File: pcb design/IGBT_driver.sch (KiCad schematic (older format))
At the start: 37 parts, among them Q13 NPN, Q14 PNP, U1 ISO5852S

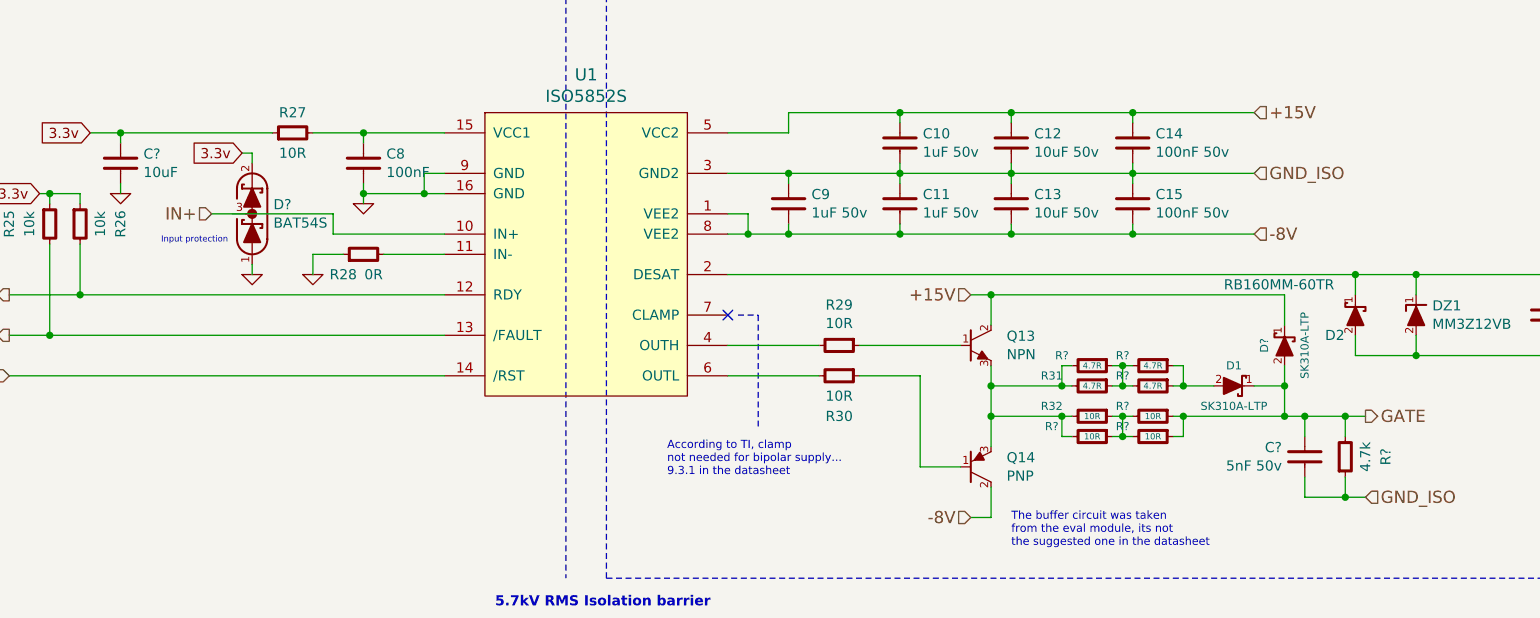
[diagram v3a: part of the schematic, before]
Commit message: Added 3D models, connector, more layout, updated readme
Signed-off-by: Marcos Chaparro <mchaparro@paltatech.com>
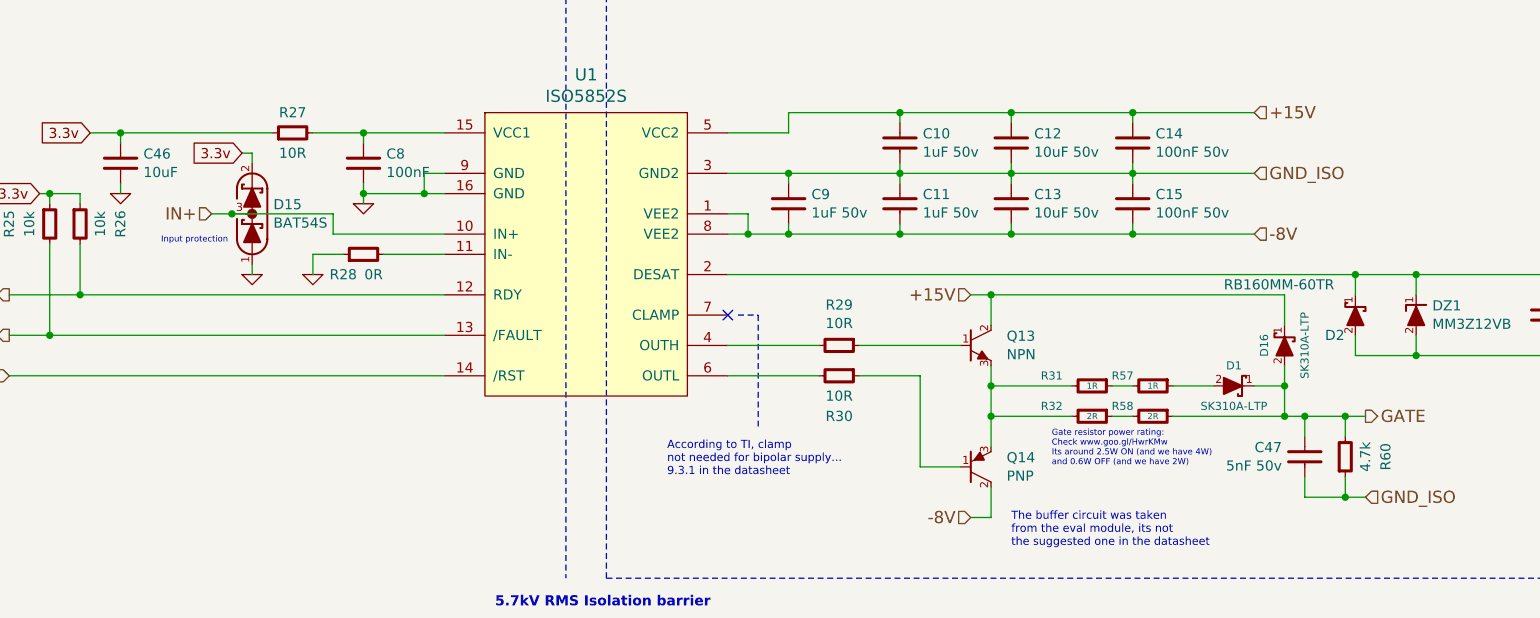
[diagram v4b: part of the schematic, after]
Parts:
- removed R? (x2): 4.7R, IPC7351-Nominal:RESC3225X60, symbol R-0805
- removed R? (x2): 10R, IPC7351-Nominal:RESC3225X60, symbol R-0805
- R31: value 4.7R -> 1R
- R32: value 10R -> 2R
- R57: renamed from R?; value 4.7R -> 1R
- R58: renamed from R?; value 10R -> 2R
- gave numbers to parts that had none: 5
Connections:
- net IN+: now also D15.3 (COM)
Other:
- note added: "Gate resistor power rating:\nCheck www.goo.gl/HwrKMw\nIts around 2.5W ON (and we have 4W)\nand 0.6W OFF (and we have 2W)"
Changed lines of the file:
@@
 	3050 4300 2750 4300
 $Comp
-L GND #PWR01
+L GND #PWR02
 U 1 1 582416B6
 P 2400 4400
-AR Path="/5822D62D/582416B6" Ref="#PWR01"  Part="1"
-AR Path="/5824556D/582416B6" Ref="#PWR014"  Part="1"
-F 0 "#PWR01" H 2400 4400 30  0001 C CNN
+AR Path="/5822D62D/582416B6" Ref="#PWR02"  Part="1"
+AR Path="/5824556D/582416B6" Ref="#PWR017"  Part="1"
+F 0 "#PWR02" H 2400 4400 30  0001 C CNN
 F 1 "GND" H 2400 4330 30  0001 C CNN
 F 2 "" H 2400 4400 60  0000 C CNN
@@
 	2950 3900 2950 4000
 $Comp
-L GND #PWR02
+L GND #PWR03
 U 1 1 58241AEC
 P 2650 4050
-AR Path="/5822D62D/58241AEC" Ref="#PWR02"  Part="1"
-AR Path="/5824556D/58241AEC" Ref="#PWR015"  Part="1"
-F 0 "#PWR02" H 2650 4050 30  0001 C CNN
+AR Path="/5822D62D/58241AEC" Ref="#PWR03"  Part="1"
+AR Path="/5824556D/58241AEC" Ref="#PWR018"  Part="1"
+F 0 "#PWR03" H 2650 4050 30  0001 C CNN
 F 1 "GND" H 2650 3980 30  0001 C CNN
 F 2 "" H 2650 4050 60  0000 C CNN
@@
 AR Path="/5824556D/5824286A" Ref="R48"  Part="1"
 F 0 "R31" V 6200 4750 40  0000 C CNN
-F 1 "4.7R" V 6250 4950 30  0000 C CNN
+F 1 "1R" V 6250 4950 30  0000 C CNN
 F 2 "IPC7351-Nominal:RESC3225X60" H 6250 4950 50  0001 C CNN
 F 3 "" H 6250 5000 60  0000 C CNN
@@
 AR Path="/5824556D/58242871" Ref="R49"  Part="1"
 F 0 "R32" V 6200 4900 40  0000 C CNN
-F 1 "10R" V 6250 5100 30  0000 C CNN
+F 1 "2R" V 6250 5100 30  0000 C CNN
 F 2 "IPC7351-Nominal:RESC3225X60" H 6250 5100 50  0001 C CNN
 F 3 "" H 6250 5150 60  0000 C CNN
@@
 	7300 5500 7300 5400
 $Comp
-L R-0805 R?
+L R-0805 R60
 U 1 1 58308678
 P 7500 5300
-AR Path="/5822D62D/58308678" Ref="R?"  Part="1"
-AR Path="/5824556D/58308678" Ref="R?"  Part="1"
-F 0 "R?" V 7700 5300 50  0000 C CNN
+AR Path="/5822D62D/58308678" Ref="R60"  Part="1"
+AR Path="/5824556D/58308678" Ref="R67"  Part="1"
+F 0 "R60" V 7700 5300 50  0000 C CNN
 F 1 "4.7k" V 7600 5300 50  0000 C CNN
 F 2 "IPC7351-Nominal:RESC2012X50" H 7500 5300 50  0001 C CNN
@@
 $EndBitmap
 $Comp
-L C-0603 C?
+L C-0603 C46
 U 1 1 5830FA22
 P 1450 3850
-AR Path="/5822D62D/5830FA22" Ref="C?"  Part="1"
-AR Path="/5824556D/5830FA22" Ref="C?"  Part="1"
-F 0 "C?" H 1563 3896 50  0000 L CNN
+AR Path="/5822D62D/5830FA22" Ref="C46"  Part="1"
+AR Path="/5824556D/5830FA22" Ref="C48"  Part="1"
+F 0 "C46" H 1563 3896 50  0000 L CNN
 F 1 "10uF" H 1563 3805 50  0000 L CNN
 F 2 "IPC7351-Nominal:CAPC1608X55" H 1450 3850 50  0001 C CNN
@@
 Connection ~ 1450 3700
 $Comp
-L GND #PWR?
+L GND #PWR04
 U 1 1 5830FC3F
 P 1450 4000
-AR Path="/5822D62D/5830FC3F" Ref="#PWR?"  Part="1"
-AR Path="/5824556D/5830FC3F" Ref="#PWR?"  Part="1"
-F 0 "#PWR?" H 1450 4000 30  0001 C CNN
+AR Path="/5822D62D/5830FC3F" Ref="#PWR04"  Part="1"
+AR Path="/5824556D/5830FC3F" Ref="#PWR019"  Part="1"
+F 0 "#PWR04" H 1450 4000 30  0001 C CNN
 F 1 "GND" H 1450 3930 30  0001 C CNN
 F 2 "" H 1450 4000 60  0000 C CNN
@@
 	1450 4000 1450 3950
 $Comp
-L BAT54S D?
+L BAT54S D15
 U 1 1 583100FD
 P 2100 4100
-AR Path="/5822D62D/583100FD" Ref="D?"  Part="1"
-AR Path="/5824556D/583100FD" Ref="D?"  Part="1"
-F 0 "D?" V 2146 3995 50  0000 R CNN
+AR Path="/5822D62D/583100FD" Ref="D15"  Part="1"
+AR Path="/5824556D/583100FD" Ref="D17"  Part="1"
+F 0 "D15" V 2146 3995 50  0000 R CNN
 F 1 "BAT54S" V 2055 3995 50  0000 R CNN
 F 2 "smd-semi:SOT-23" H 2100 3950 60  0001 C CNN
@@
 	2100 3800 2100 3850
 $Comp
-L GND #PWR?
+L GND #PWR05
 U 1 1 58310421
 P 2100 4400
-AR Path="/5822D62D/58310421" Ref="#PWR?"  Part="1"
-AR Path="/5824556D/58310421" Ref="#PWR?"  Part="1"
-F 0 "#PWR?" H 2100 4400 30  0001 C CNN
+AR Path="/5822D62D/58310421" Ref="#PWR05"  Part="1"
+AR Path="/5824556D/58310421" Ref="#PWR020"  Part="1"
+F 0 "#PWR05" H 2100 4400 30  0001 C CNN
 F 1 "GND" H 2100 4330 30  0001 C CNN
 F 2 "" H 2100 4400 60  0000 C CNN
@@
 P 7300 5300
 AR Path="/58232371/58307C69" Ref="C?"  Part="1"
-AR Path="/5822D62D/58307C69" Ref="C?"  Part="1"
-AR Path="/5824556D/58307C69" Ref="C?"  Part="1"
-F 0 "C?" H 7413 5346 50  0000 L CNN
+AR Path="/5822D62D/58307C69" Ref="C47"  Part="1"
+AR Path="/5824556D/58307C69" Ref="C49"  Part="1"
+F 0 "C47" H 7413 5346 50  0000 L CNN
 F 1 "5nF 50v" H 7413 5255 50  0000 L CNN
 F 2 "IPC7351-Nominal:CAPC2012X70" H 7300 5300 50  0001 C CNN
@@
 $EndComp
 $Comp
-L R-0805 R?
-U 1 1 5832B661
-P 6250 4850
-AR Path="/5822D62D/5832B661" Ref="R?"  Part="1"
-AR Path="/5824556D/5832B661" Ref="R?"  Part="1"
-F 0 "R?" V 6200 4700 40  0000 C CNN
-F 1 "4.7R" V 6250 4850 30  0000 C CNN
-F 2 "IPC7351-Nominal:RESC3225X60" H 6250 4850 50  0001 C CNN
-F 3 "" H 6250 4900 60  0000 C CNN
-F 4 "RES SMD 1k 5% [2512]" H 7000 5400 60  0001 C CNN "BOM"
-	1    6250 4850
-	0    1    1    0
-$EndComp
-Wire Wire Line
-	6150 4850 6100 4850
-Wire Wire Line
-	6100 4850 6100 4950
-Connection ~ 6100 4950
-Wire Wire Line
-	6350 4850 6450 4850
-Wire Wire Line
-	6400 4850 6400 4950
-$Comp
-L R-0805 R?
-U 1 1 5832BA90
-P 6250 5200
-AR Path="/5822D62D/5832BA90" Ref="R?"  Part="1"
-AR Path="/5824556D/5832BA90" Ref="R?"  Part="1"
-F 0 "R?" V 6200 5000 40  0000 C CNN
-F 1 "10R" V 6250 5200 30  0000 C CNN
-F 2 "IPC7351-Nominal:RESC3225X60" H 6250 5200 50  0001 C CNN
-F 3 "" H 6250 5250 60  0000 C CNN
-F 4 "RES SMD 1k 5% [2512]" H 7000 5750 60  0001 C CNN "BOM"
-	1    6250 5200
-	0    1    1    0
-$EndComp
-Wire Wire Line
-	6150 5200 6100 5200
-Wire Wire Line
-	6100 5200 6100 5100
-Connection ~ 6100 5100
-Wire Wire Line
-	6350 5200 6450 5200
-Wire Wire Line
-	6400 5200 6400 5100
-$Comp
-L R-0805 R?
-U 1 1 5832CE45
-P 6550 4850
-AR Path="/5822D62D/5832CE45" Ref="R?"  Part="1"
-AR Path="/5824556D/5832CE45" Ref="R?"  Part="1"
-F 0 "R?" V 6500 4700 40  0000 C CNN
-F 1 "4.7R" V 6550 4850 30  0000 C CNN
-F 2 "IPC7351-Nominal:RESC3225X60" H 6550 4850 50  0001 C CNN
-F 3 "" H 6550 4900 60  0000 C CNN
-F 4 "RES SMD 1k 5% [2512]" H 7300 5400 60  0001 C CNN "BOM"
-	1    6550 4850
-	0    1    1    0
-$EndComp
-Connection ~ 6400 4850
-$Comp
-L R-0805 R?
+L R-0805 R57
 U 1 1 5832D091
 P 6550 4950
-AR Path="/5822D62D/5832D091" Ref="R?"  Part="1"
-AR Path="/5824556D/5832D091" Ref="R?"  Part="1"
-F 0 "R?" V 6500 4800 40  0000 C CNN
-F 1 "4.7R" V 6550 4950 30  0000 C CNN
+AR Path="/5822D62D/5832D091" Ref="R57"  Part="1"
+AR Path="/5824556D/5832D091" Ref="R64"  Part="1"
+F 0 "R57" V 6500 4800 40  0000 C CNN
+F 1 "1R" V 6550 4950 30  0000 C CNN
 F 2 "IPC7351-Nominal:RESC3225X60" H 6550 4950 50  0001 C CNN
 F 3 "" H 6550 5000 60  0000 C CNN
@@
 	0    1    1    0
 $EndComp
-Connection ~ 6400 4950
 Wire Wire Line
 	6650 4950 6850 4950
-Wire Wire Line
-	6650 4850 6700 4850
-Wire Wire Line
-	6700 4850 6700 4950
-Connection ~ 6700 4950
 $Comp
-L R-0805 R?
+L R-0805 R58
 U 1 1 5832D475
 P 6550 5100
-AR Path="/5822D62D/5832D475" Ref="R?"  Part="1"
-AR Path="/5824556D/5832D475" Ref="R?"  Part="1"
-F 0 "R?" V 6500 4950 40  0000 C CNN
-F 1 "10R" V 6550 5100 30  0000 C CNN
+AR Path="/5822D62D/5832D475" Ref="R58"  Part="1"
+AR Path="/5824556D/5832D475" Ref="R65"  Part="1"
+F 0 "R58" V 6500 4950 40  0000 C CNN
+F 1 "2R" V 6550 5100 30  0000 C CNN
 F 2 "IPC7351-Nominal:RESC3225X60" H 6550 5100 50  0001 C CNN
 F 3 "" H 6550 5150 60  0000 C CNN
@@
 	0    1    1    0
 $EndComp
-Connection ~ 6400 5100
-$Comp
-L R-0805 R?
-U 1 1 5832D63E
-P 6550 5200
-AR Path="/5822D62D/5832D63E" Ref="R?"  Part="1"
-AR Path="/5824556D/5832D63E" Ref="R?"  Part="1"
-F 0 "R?" V 6500 5050 40  0000 C CNN
-F 1 "10R" V 6550 5200 30  0000 C CNN
-F 2 "IPC7351-Nominal:RESC3225X60" H 6550 5200 50  0001 C CNN
-F 3 "" H 6550 5250 60  0000 C CNN
-F 4 "RES SMD 1k 5% [2512]" H 7300 5750 60  0001 C CNN "BOM"
-	1    6550 5200
-	0    1    1    0
-$EndComp
-Connection ~ 6400 5200
-Wire Wire Line
-	6650 5200 6700 5200
-Wire Wire Line
-	6700 5200 6700 5100
 Connection ~ 7200 5100
-Connection ~ 6700 5100
 Text Notes 4150 5400 0    40   ~ 0
 According to TI, clamp\nnot needed for bipolar supply...\n9.3.1 in the datasheet
@@
 	4600 4600 4600 5150
 $Comp
-L SCHOTTKY D?
+L SCHOTTKY D16
 U 1 1 5833272F
 P 7200 4750
-F 0 "D?" V 7300 4750 40  0000 C CNN
+AR Path="/5822D62D/5833272F" Ref="D16"  Part="1"
+AR Path="/5824556D/5833272F" Ref="D18"  Part="1"
+F 0 "D16" V 7300 4750 40  0000 C CNN
 F 1 "SK310A-LTP" V 7100 4750 40  0000 C CNN
 F 2 "w_smd_diode:do214ac" H 7200 4750 60  0001 C CNN
@@
 	7200 4500 7200 4650
 Connection ~ 5750 4500
+Connection ~ 2000 4100
+Text Notes 6050 5350 0    30   ~ 0
+Gate resistor power rating:\nCheck www.goo.gl/HwrKMw\nIts around 2.5W ON (and we have 4W)\nand 0.6W OFF (and we have 2W)
 $EndSCHEMATC

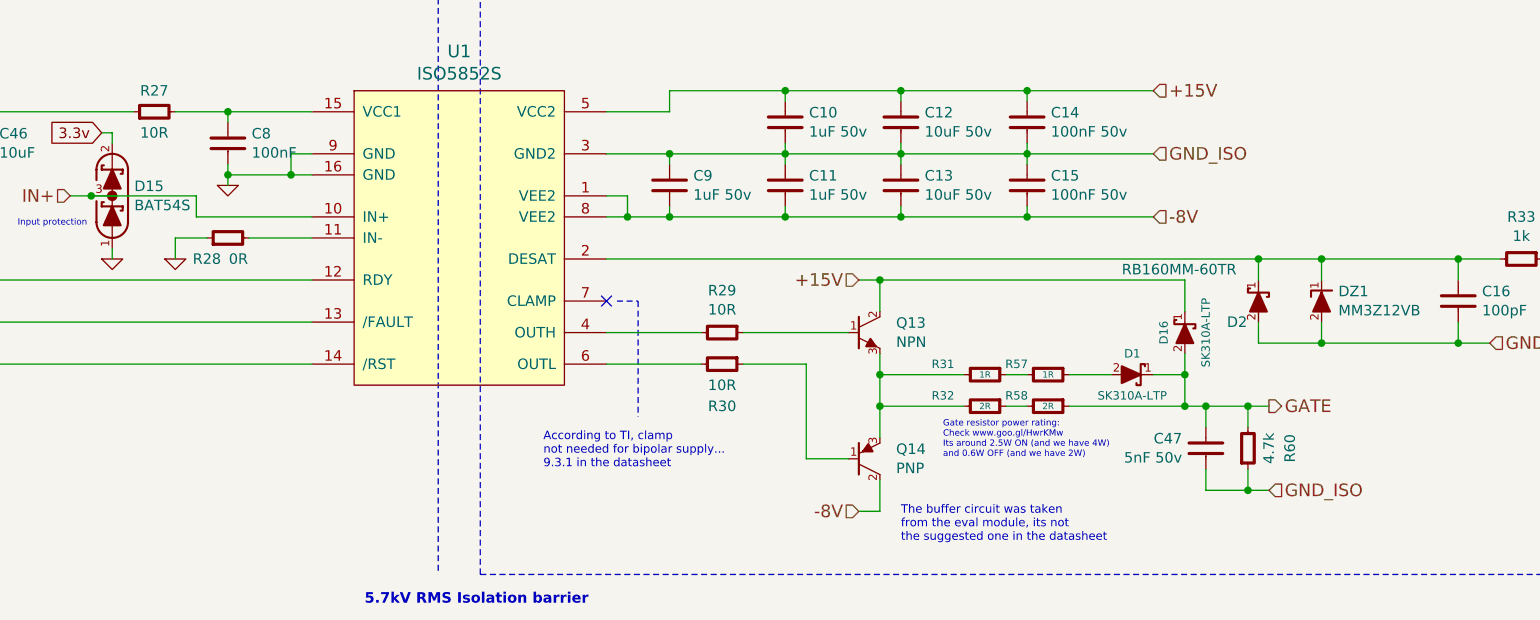
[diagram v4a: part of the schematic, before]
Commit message: Added testpoints
Signed-off-by: Marcos Chaparro <mchaparro@paltatech.com>
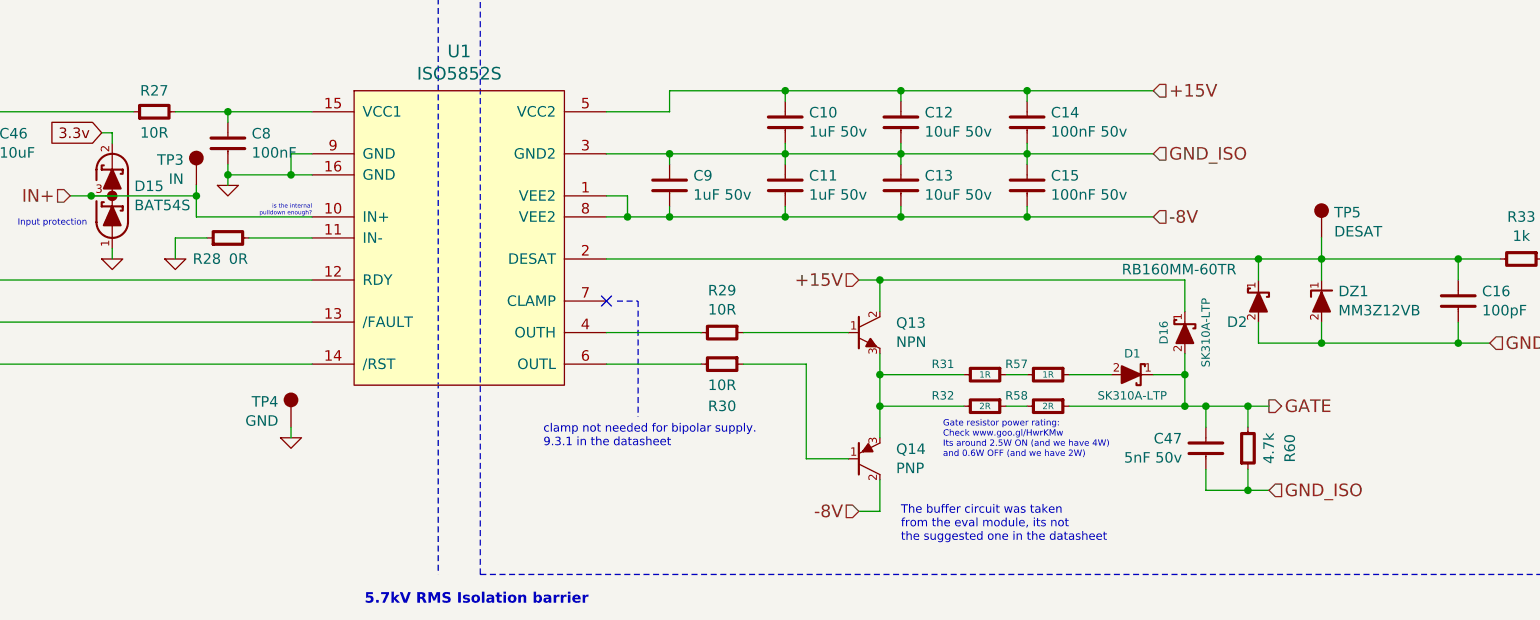
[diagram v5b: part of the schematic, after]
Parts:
- added TP3: IN, conn-test:TEST-SMD-SMALL, symbol TESTPOINT
- added TP4: GND, conn-test:TEST-SMD-SMALL, symbol TESTPOINT
- added TP5: DESAT, conn-test:TEST-SMD-SMALL, symbol TESTPOINT
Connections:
- net GND: now also TP4.1
- net IN+: now also TP3.1
- net at C16.1, D2.1 (K), DZ1.1 (K)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: now also TP5.1
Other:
- note added: "clamp not needed for bipolar supply.\n9.3.1 in the datasheet"
- note added: "is the internal\npulldown enough?"
- note removed: "According to TI, clamp\nnot needed for bipolar supply...\n9.3.1 in the datasheet"

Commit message: Change gate diode direction, I thought Ron should be smaller than Roff, and its not
Signed-off-by: Marcos Chaparro <mchaparro@paltatech.com>
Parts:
- removed R28: 0R, IPC7351-Nominal:RESC1608X50, symbol R-0603
- added J2: DESAT, conn-100mil:CONN-100MIL-F-1x1, symbol CONN-100MIL-F-1x1
- added R?: 10k, IPC7351-Nominal:RESC1608X50, symbol R-0603
- added U?: SN74AUC1G14, smd-semi:SOT-23-5, symbol 741G04-SOT23
- R31, R57: value 1R -> 2R
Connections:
- wire segments 82 -> 84
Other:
- note added: "Global Shutdown and reset configuration.\nEnsures that when ANY driver faults, all of\nthem are turned off"
- note added: "TH to connect to\ncopper collector layer"
- note removed: "is the internal\npulldown enough?"
- moved on the sheet: C10, C11, C12, C13, C14, C15, C16, C46, C47, C8, C9, D1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
